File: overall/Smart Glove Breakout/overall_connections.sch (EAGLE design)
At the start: 1 part

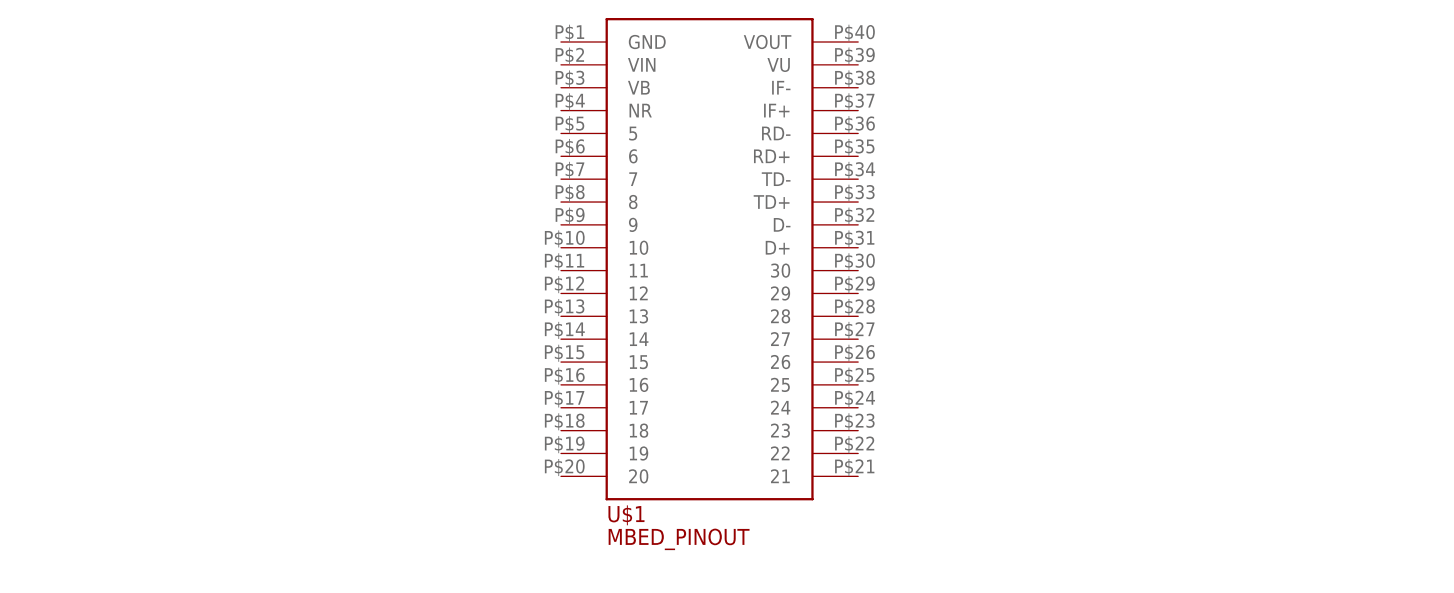
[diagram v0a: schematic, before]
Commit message: Updated Library of IC pinouts
Includes the pinouts for the MPR121 Capacitive Touch Sensor breakout
board and the Huzzah ESP breakout board.
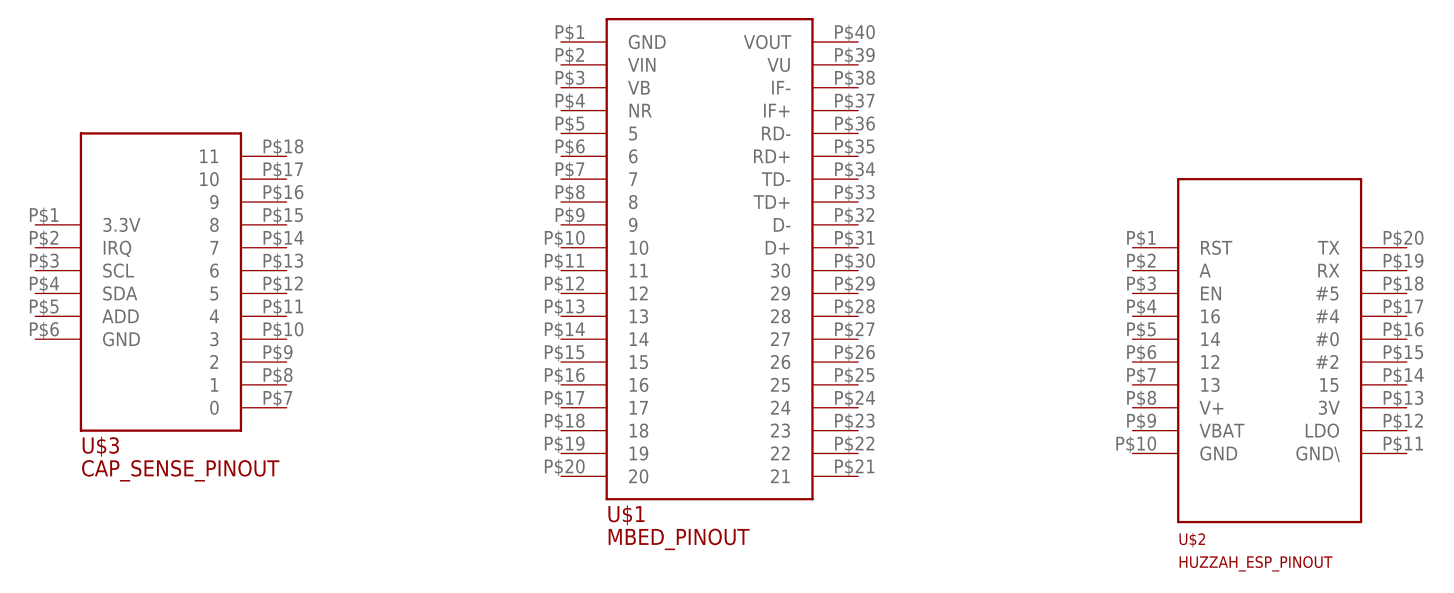
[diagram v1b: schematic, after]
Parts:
- added U$2: HUZZAH_ESP_PINOUT, smart_glove_breakout:HUZZAH_ESP_PINOUT
- added U$3: CAP_SENSE_PINOUT, smart_glove_breakout:CAP_SENSE_PINOUT
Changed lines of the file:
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@@
 <parts>
 <part name="U$1" library="smart_glove_breakout" deviceset="MBED_PINOUT" device=""/>
+<part name="U$2" library="smart_glove_breakout" deviceset="HUZZAH_ESP_PINOUT" device=""/>
+<part name="U$3" library="smart_glove_breakout" deviceset="CAP_SENSE_PINOUT" device=""/>
 </parts>
 <sheets>
@@
 <instances>
 <instance part="U$1" gate="G$1" x="0" y="0"/>
+<instance part="U$2" gate="G$1" x="63.5" y="-15.24"/>
+<instance part="U$3" gate="G$1" x="-58.42" y="-12.7"/>
 </instances>
 <busses>
